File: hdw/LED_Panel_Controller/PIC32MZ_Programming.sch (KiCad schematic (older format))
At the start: 17 parts

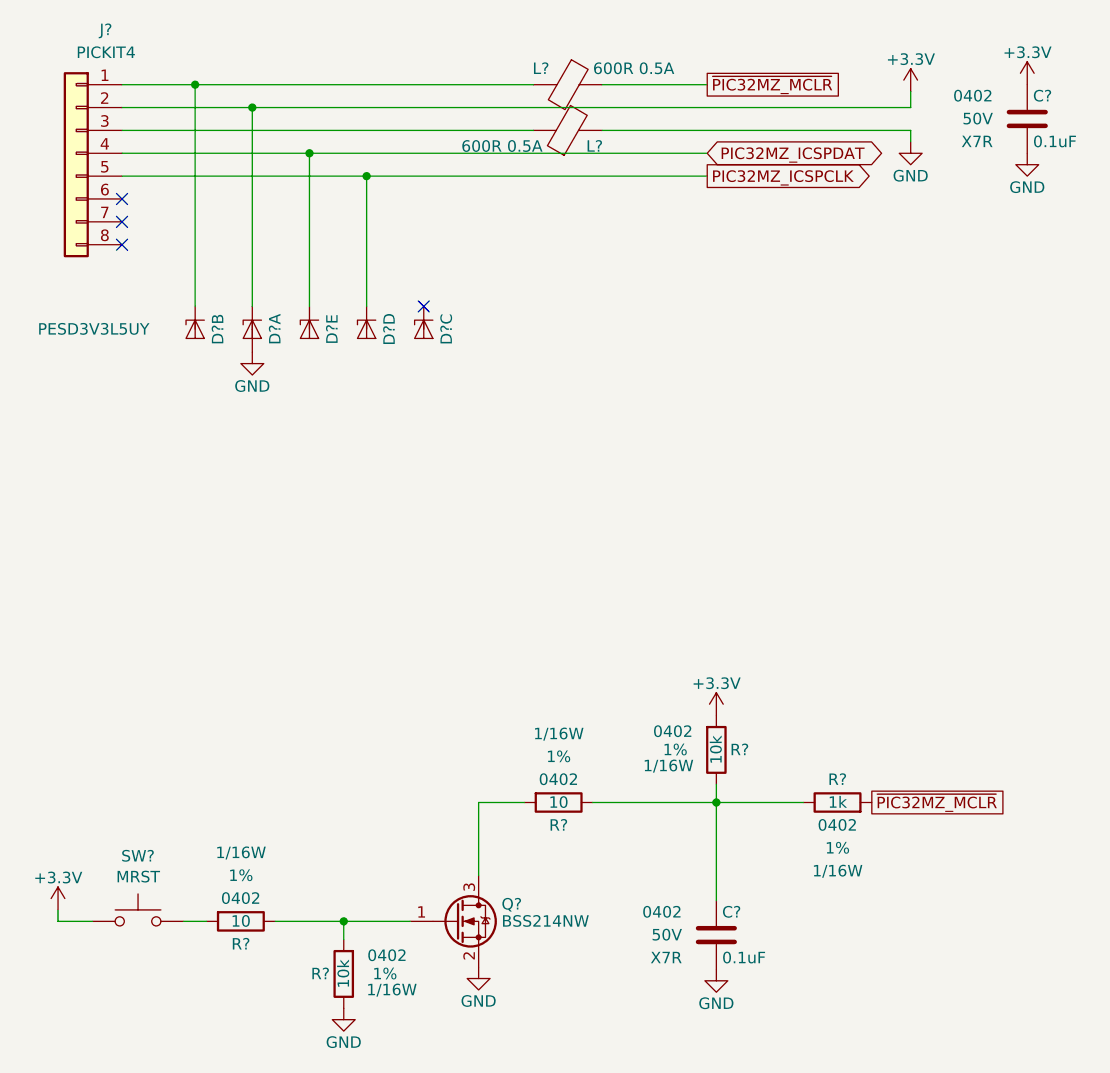
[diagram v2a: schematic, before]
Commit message: added digikey pns, footprints, bom scrubbed
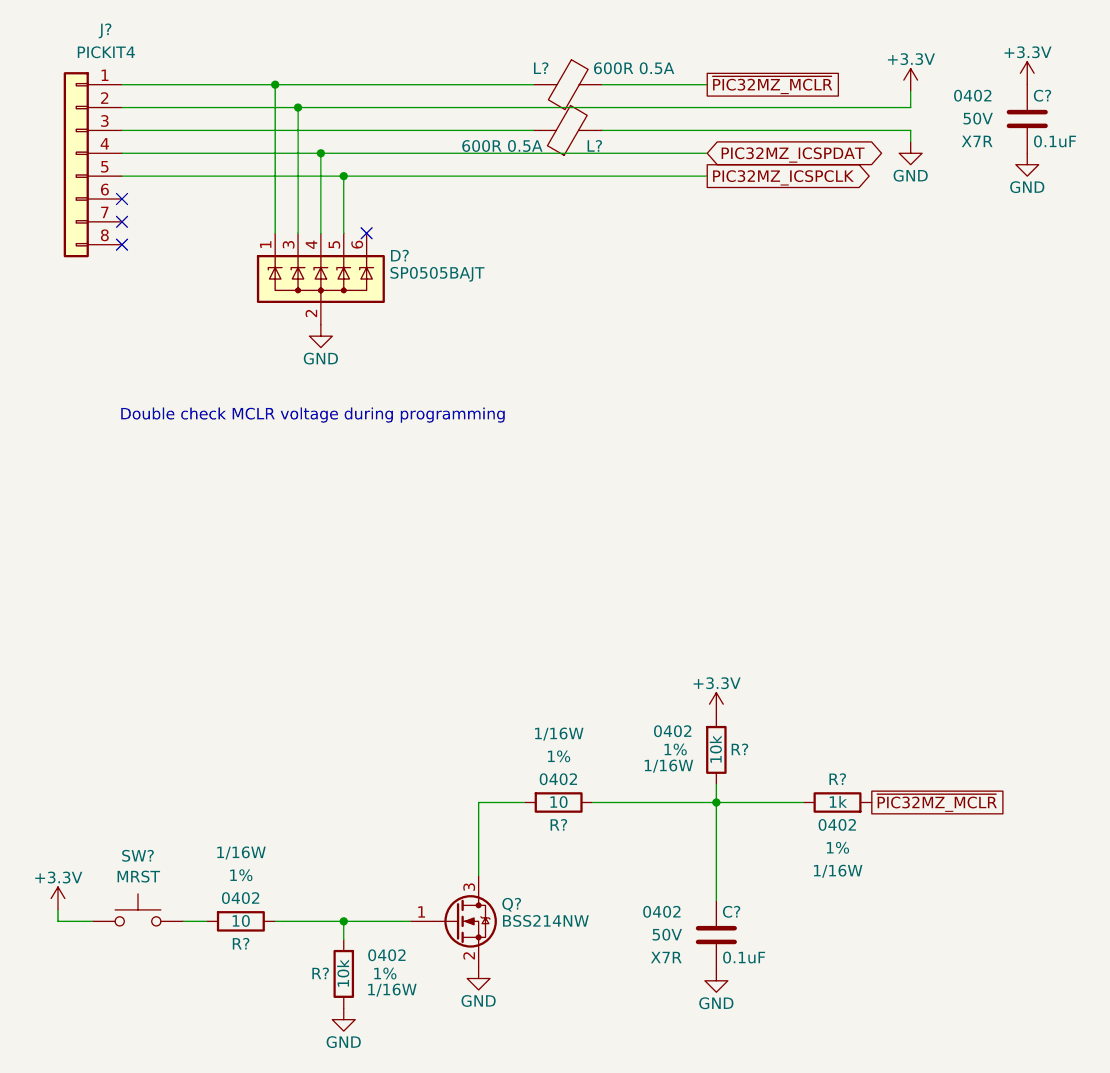
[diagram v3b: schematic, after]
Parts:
- removed D? (x5): PESD3V3L5UY, Package_TO_SOT_SMD:SOT-363_SC-70-6, symbol Power_Protection:PESD3V3L5UY
- added D?: SP0505BAJT, TO_SOT_Packages_SMD:SOT-363_SC-70-6, symbol Power_Protection:SP0505BAJT
- C? (x2): footprint (none) -> Capacitors_SMD:C_0402; Digi-Key PN (none) -> 490-10701-1-ND
- J?: Configuration (none) -> DEV
- R? (x2): Digi-Key PN (none) -> RMCF0402FT10K0CT-ND
- R?: Digi-Key PN (none) -> RMCF0402FT1K00CT-ND
- R? (x2): Digi-Key PN (none) -> RMCF0402FT10R0CT-ND
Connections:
- net +3V3: now also D?.3 (K)
- net GND: now also D?.2 (A)
- net PIC32MZ_ICSPCLK: now also D?.5 (K)
- net PIC32MZ_ICSPDAT: now also D?.4 (K)
- net at J?.1 (Pin_1), L?.2: now also D?.1 (K)
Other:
- note added: "Double check MCLR voltage during programming"
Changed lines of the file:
@@
 F 0 "C?" H 7155 2110 50  0000 L CNN
 F 1 "0.1uF" H 7155 1910 50  0000 L CNN
-F 2 "" H 7168 1860 50  0001 C CNN
+F 2 "Capacitors_SMD:C_0402" H 7168 1860 50  0001 C CNN
 F 3 "" H 7155 2110 50  0001 C CNN
 F 4 "0402" H 6980 2110 50  0000 R CNN "display_footprint"
 F 5 "50V" H 6980 2010 50  0000 R CNN "Voltage"
 F 6 "X7R" H 6980 1910 50  0000 R CNN "Dielectric"
-F 7 "" H 7555 2510 60  0001 C CNN "Digi-Key PN"
+F 7 "490-10701-1-ND" H 7555 2510 60  0001 C CNN "Digi-Key PN"
 	1    7130 2010
 	1    0    0    -1
@@
 F 5 "1%" H 5950 4770 50  0000 C CNN "Tolerance"
 F 6 "1/16W" H 5980 4700 50  0000 C CNN "Wattage"
-F 7 "" H 6070 5170 60  0001 C CNN "Digi-Key PN"
+F 7 "RMCF0402FT10K0CT-ND" H 6070 5170 60  0001 C CNN "Digi-Key PN"
 	1    5770 4770
 	-1   0    0    -1
@@
 F 0 "C?" H 5795 5680 50  0000 L CNN
 F 1 "0.1uF" H 5795 5480 50  0000 L CNN
-F 2 "" H 5808 5430 50  0001 C CNN
+F 2 "Capacitors_SMD:C_0402" H 5808 5430 50  0001 C CNN
 F 3 "" H 5795 5680 50  0001 C CNN
 F 4 "0402" H 5620 5680 50  0000 R CNN "display_footprint"
 F 5 "50V" H 5620 5580 50  0000 R CNN "Voltage"
 F 6 "X7R" H 5620 5480 50  0000 R CNN "Dielectric"
-F 7 "" H 6195 6080 60  0001 C CNN "Digi-Key PN"
+F 7 "490-10701-1-ND" H 6195 6080 60  0001 C CNN "Digi-Key PN"
 	1    5770 5580
 	1    0    0    -1
@@
 F 5 "1%" V 6500 5000 50  0000 C CNN "Tolerance"
 F 6 "1/16W" V 6600 5000 50  0000 C CNN "Wattage"
-F 7 "" H 6600 5400 60  0001 C CNN "Digi-Key PN"
+F 7 "RMCF0402FT1K00CT-ND" H 6600 5400 60  0001 C CNN "Digi-Key PN"
 	1    6300 5000
 	0    1    1    0
@@
 F 5 "1%" V 3890 5520 50  0000 C CNN "Tolerance"
 F 6 "1/16W" V 3990 5520 50  0000 C CNN "Wattage"
-F 7 "" H 3990 5920 60  0001 C CNN "Digi-Key PN"
+F 7 "RMCF0402FT10R0CT-ND" H 3990 5920 60  0001 C CNN "Digi-Key PN"
 	1    3690 5520
 	0    -1   -1   0
@@
 F 5 "1%" H 4320 5750 50  0000 C CNN "Tolerance"
 F 6 "1/16W" H 4350 5680 50  0000 C CNN "Wattage"
-F 7 "" H 4440 6150 60  0001 C CNN "Digi-Key PN"
+F 7 "RMCF0402FT10K0CT-ND" H 4440 6150 60  0001 C CNN "Digi-Key PN"
 	1    4140 5750
 	1    0    0    -1
@@
 F 2 "Custom Footprints Library:PICKIT4_Header" H 2970 2160 50  0001 C CNN
 F 3 "~" H 2970 2160 50  0001 C CNN
+F 4 "DEV" H 2970 2160 50  0001 C CNN "Configuration"
 	1    2970 2160
 	-1   0    0    -1
@@
 NoConn ~ 3170 2460
 NoConn ~ 3170 2560
-$Comp
-L Power_Protection:PESD3V3L5UY D?
-U 1 1 5F37FACB
-P 3740 2930
-F 0 "D?" H 3740 3030 50  0000 C CNN
-F 1 "PESD3V3L5UY" V 3740 2480 50  0000 R CNN
-F 2 "Package_TO_SOT_SMD:SOT-363_SC-70-6" H 3740 2930 50  0001 C CNN
-F 3 "https://assets.nexperia.com/documents/data-sheet/PESDXL5UF_V_Y.pdf" H 3740 2930 50  0001 C CNN
-F 4 "1727-3828-1-ND" H 3740 2930 50  0001 C CNN "Digi-Key PN"
-	1    3740 2930
-	0    1    1    0
-$EndComp
-$Comp
-L Power_Protection:PESD3V3L5UY D?
-U 3 1 5F380F72
-P 4490 2930
-F 0 "D?" H 4490 3030 50  0000 C CNN
-F 1 "PESD3V3L5UY" H 4490 2830 50  0001 C CNN
-F 2 "Package_TO_SOT_SMD:SOT-363_SC-70-6" H 4490 2930 50  0001 C CNN
-F 3 "https://assets.nexperia.com/documents/data-sheet/PESDXL5UF_V_Y.pdf" H 4490 2930 50  0001 C CNN
-F 4 "1727-3828-1-ND" H 4490 2930 50  0001 C CNN "Digi-Key PN"
-	3    4490 2930
-	0    1    1    0
-$EndComp
-$Comp
-L Power_Protection:PESD3V3L5UY D?
-U 4 1 5F381590
-P 4240 2930
-F 0 "D?" H 4240 3030 50  0000 C CNN
-F 1 "PESD3V3L5UY" H 4240 2830 50  0001 C CNN
-F 2 "Package_TO_SOT_SMD:SOT-363_SC-70-6" H 4240 2930 50  0001 C CNN
-F 3 "https://assets.nexperia.com/documents/data-sheet/PESDXL5UF_V_Y.pdf" H 4240 2930 50  0001 C CNN
-F 4 "1727-3828-1-ND" H 4240 2930 50  0001 C CNN "Digi-Key PN"
-	4    4240 2930
-	0    1    1    0
-$EndComp
-$Comp
-L power:GND #PWR?
-U 1 1 5F3831ED
-P 3740 3030
-F 0 "#PWR?" H 3740 2780 50  0001 C CNN
-F 1 "GND" H 3740 2880 50  0000 C CNN
-F 2 "" H 3740 3030 50  0001 C CNN
-F 3 "" H 3740 3030 50  0001 C CNN
-	1    3740 3030
-	-1   0    0    -1
-$EndComp
 $Comp
 L Device:Ferrite_Bead L?
@@
 	5270 2060 6620 2060
 Wire Wire Line
-	3170 1960 3740 1960
-Wire Wire Line
-	3170 1860 3490 1860
-Wire Wire Line
-	3170 2160 3990 2160
-Wire Wire Line
-	3490 2830 3490 1860
-Wire Wire Line
-	3740 2830 3740 1960
-Wire Wire Line
-	3990 2830 3990 2160
-Wire Wire Line
-	4240 2830 4240 2260
-Wire Wire Line
-	4240 2260 3170 2260
-NoConn ~ 4490 2830
-Wire Wire Line
-	3490 1860 4970 1860
-Connection ~ 3490 1860
-Wire Wire Line
-	3740 1960 6620 1960
-Connection ~ 3740 1960
-Wire Wire Line
 	4970 2060 3170 2060
-Wire Wire Line
-	3990 2160 5730 2160
-Connection ~ 3990 2160
-Wire Wire Line
-	5730 2260 4240 2260
-Connection ~ 4240 2260
 Wire Wire Line
 	4730 5000 4930 5000
@@
 F 5 "1%" V 5280 5000 50  0000 C CNN "Tolerance"
 F 6 "1/16W" V 5380 5000 50  0000 C CNN "Wattage"
-F 7 "" H 5380 5400 60  0001 C CNN "Digi-Key PN"
+F 7 "RMCF0402FT10R0CT-ND" H 5380 5400 60  0001 C CNN "Digi-Key PN"
 	1    5080 5000
 	0    -1   -1   0
 $EndComp
-$Comp
-L Power_Protection:PESD3V3L5UY D?
-U 5 1 5F39050C
-P 3990 2930
-F 0 "D?" H 3990 3030 50  0000 C CNN
-F 1 "PESD3V3L5UY" H 3990 2830 50  0001 C CNN
-F 2 "Package_TO_SOT_SMD:SOT-363_SC-70-6" H 3990 2930 50  0001 C CNN
-F 3 "https://assets.nexperia.com/documents/data-sheet/PESDXL5UF_V_Y.pdf" H 3990 2930 50  0001 C CNN
-F 4 "1727-3828-1-ND" H 3990 2930 50  0001 C CNN "Digi-Key PN"
-	5    3990 2930
-	0    1    1    0
-$EndComp
-$Comp
-L Power_Protection:PESD3V3L5UY D?
-U 2 1 5F38087E
-P 3490 2930
-F 0 "D?" H 3490 3030 50  0000 C CNN
-F 1 "PESD3V3L5UY" H 3490 2830 50  0001 C CNN
-F 2 "Package_TO_SOT_SMD:SOT-363_SC-70-6" H 3490 2930 50  0001 C CNN
-F 3 "https://assets.nexperia.com/documents/data-sheet/PESDXL5UF_V_Y.pdf" H 3490 2930 50  0001 C CNN
-F 4 "1727-3828-1-ND" H 3490 2930 50  0001 C CNN "Digi-Key PN"
-	2    3490 2930
-	0    1    1    0
-$EndComp
+Wire Wire Line
+	3170 2160 4040 2160
+Wire Wire Line
+	3170 2260 4140 2260
+$Comp
+L Power_Protection:SP0505BAJT D?
+U 1 1 6067D672
+P 4040 2710
+AR Path="/5F583BFC/6067D672" Ref="D?"  Part="1"
+AR Path="/5F5829A6/6067D672" Ref="D?"  Part="1"
+F 0 "D?" H 4340 2810 50  0000 L CNN
+F 1 "SP0505BAJT" H 4340 2735 50  0000 L CNN
+F 2 "TO_SOT_Packages_SMD:SOT-363_SC-70-6" H 4340 2660 50  0001 L CNN
+F 3 "http://www.littelfuse.com/~/media/files/littelfuse/technical%20resources/documents/data%20sheets/sp05xxba.pdf" H 4165 2835 50  0001 C CNN
+F 4 "F3160CT-ND" H 4040 2710 50  0001 C CNN "Digi-Key PN"
+	1    4040 2710
+	1    0    0    -1
+$EndComp
+$Comp
+L power:GND #PWR?
+U 1 1 6067E0F5
+P 4040 2910
+F 0 "#PWR?" H 4040 2660 50  0001 C CNN
+F 1 "GND" H 4040 2760 50  0000 C CNN
+F 2 "" H 4040 2910 50  0001 C CNN
+F 3 "" H 4040 2910 50  0001 C CNN
+	1    4040 2910
+	1    0    0    -1
+$EndComp
+Wire Wire Line
+	3170 1860 3840 1860
+Wire Wire Line
+	3170 1960 3940 1960
+Wire Wire Line
+	3940 2510 3940 1960
+Connection ~ 3940 1960
+Wire Wire Line
+	3940 1960 6620 1960
+Wire Wire Line
+	4040 2510 4040 2160
+Connection ~ 4040 2160
+Wire Wire Line
+	4040 2160 5730 2160
+Wire Wire Line
+	4140 2510 4140 2260
+Connection ~ 4140 2260
+Wire Wire Line
+	4140 2260 5730 2260
+Wire Wire Line
+	3840 2510 3840 1860
+Connection ~ 3840 1860
+Wire Wire Line
+	3840 1860 4970 1860
+NoConn ~ 4240 2510
+Text Notes 3160 3340 0    50   ~ 0
+Double check MCLR voltage during programming
 $EndSCHEMATC

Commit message: assigned I2C addresses
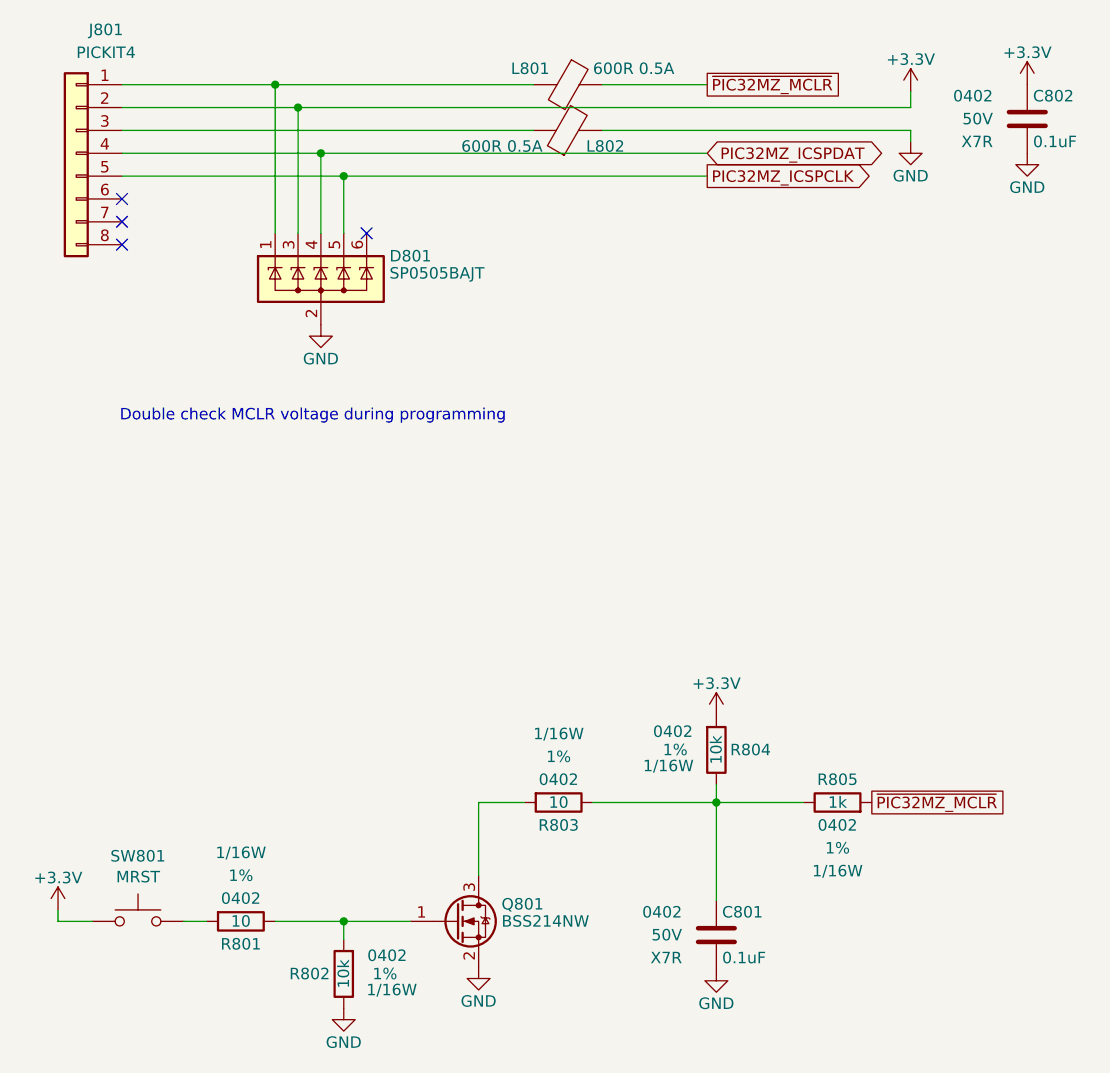
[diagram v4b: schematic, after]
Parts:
- gave numbers to parts that had none: 13
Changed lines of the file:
@@
 PIC32MZ_ICSPCLK
 $Comp
-L power:GND #PWR?
+L power:GND #PWR0808
 U 1 1 5BB4A7C4
 P 6620 2110
-F 0 "#PWR?" H 6620 1860 50  0001 C CNN
+F 0 "#PWR0808" H 6620 1860 50  0001 C CNN
 F 1 "GND" H 6620 1960 50  0000 C CNN
 F 2 "" H 6620 2110 50  0001 C CNN
@@
 NoConn ~ 3170 2360
 $Comp
-L Custom_Library:C_Custom C?
+L Custom_Library:C_Custom C802
 U 1 1 5BC13497
 P 7130 2010
-F 0 "C?" H 7155 2110 50  0000 L CNN
+F 0 "C802" H 7155 2110 50  0000 L CNN
 F 1 "0.1uF" H 7155 1910 50  0000 L CNN
 F 2 "Capacitors_SMD:C_0402" H 7168 1860 50  0001 C CNN
@@
 $EndComp
 $Comp
-L power:GND #PWR?
+L power:GND #PWR0810
 U 1 1 5BC1349E
 P 7130 2160
-F 0 "#PWR?" H 7130 1910 50  0001 C CNN
+F 0 "#PWR0810" H 7130 1910 50  0001 C CNN
 F 1 "GND" H 7130 2010 50  0000 C CNN
 F 2 "" H 7130 2160 50  0001 C CNN
@@
 AR Path="/5EAE2EF2/5BC152E5" Ref="R?"  Part="1"
 AR Path="/5E939EAF/5BC152E5" Ref="R?"  Part="1"
-AR Path="/5F5829A6/5BC152E5" Ref="R?"  Part="1"
-F 0 "R?" H 5710 4770 50  0000 R CNN
+AR Path="/5F5829A6/5BC152E5" Ref="R804"  Part="1"
+F 0 "R804" H 5710 4770 50  0000 R CNN
 F 1 "10k" V 5770 4770 50  0000 C CNN
 F 2 "Resistors_SMD:R_0402" H 5770 4770 50  0001 C CNN
@@
 $EndComp
 $Comp
-L Custom_Library:C_Custom C?
+L Custom_Library:C_Custom C801
 U 1 1 5BC1574E
 P 5770 5580
-F 0 "C?" H 5795 5680 50  0000 L CNN
+F 0 "C801" H 5795 5680 50  0000 L CNN
 F 1 "0.1uF" H 5795 5480 50  0000 L CNN
 F 2 "Capacitors_SMD:C_0402" H 5808 5430 50  0001 C CNN
@@
 $EndComp
 $Comp
-L power:GND #PWR?
+L power:GND #PWR0806
 U 1 1 5BC15E18
 P 5770 5730
-F 0 "#PWR?" H 5770 5480 50  0001 C CNN
+F 0 "#PWR0806" H 5770 5480 50  0001 C CNN
 F 1 "GND" H 5770 5580 50  0000 C CNN
 F 2 "" H 5770 5730 50  0001 C CNN
@@
 $EndComp
 $Comp
-L Custom_Library:R_Custom R?
+L Custom_Library:R_Custom R805
 U 1 1 5BC16316
 P 6300 5000
-F 0 "R?" V 6200 5000 50  0000 C CNN
+F 0 "R805" V 6200 5000 50  0000 C CNN
 F 1 "1k" V 6300 5000 50  0000 C CNN
 F 2 "Resistors_SMD:R_0402" H 6300 5000 50  0001 C CNN
@@
 ~PIC32MZ_MCLR
 $Comp
-L Switch:SW_Push SW?
+L Switch:SW_Push SW801
 U 1 1 5BC17B44
 P 3240 5520
-F 0 "SW?" H 3240 5805 50  0000 C CNN
+F 0 "SW801" H 3240 5805 50  0000 C CNN
 F 1 "MRST" H 3240 5714 50  0000 C CNN
 F 2 "Buttons_Switches_THT:SW_PUSH_6mm" H 3240 5720 50  0001 C CNN
@@
 $EndComp
 $Comp
-L power:GND #PWR?
+L power:GND #PWR0804
 U 1 1 5BE087C1
 P 4730 5720
-F 0 "#PWR?" H 4730 5470 50  0001 C CNN
+F 0 "#PWR0804" H 4730 5470 50  0001 C CNN
 F 1 "GND" H 4730 5570 50  0000 C CNN
 F 2 "" H 4730 5720 50  0001 C CNN
@@
 $EndComp
 $Comp
-L Custom_Library:R_Custom R?
+L Custom_Library:R_Custom R801
 U 1 1 5BE087CB
 P 3690 5520
-F 0 "R?" V 3590 5520 50  0000 C CNN
+F 0 "R801" V 3590 5520 50  0000 C CNN
 F 1 "10" V 3690 5520 50  0000 C CNN
 F 2 "Resistors_SMD:R_0402" H 3690 5520 50  0001 C CNN
@@
 AR Path="/5EAE2EF2/5BE087D6" Ref="R?"  Part="1"
 AR Path="/5E939EAF/5BE087D6" Ref="R?"  Part="1"
-AR Path="/5F5829A6/5BE087D6" Ref="R?"  Part="1"
-F 0 "R?" H 4080 5750 50  0000 R CNN
+AR Path="/5F5829A6/5BE087D6" Ref="R802"  Part="1"
+F 0 "R802" H 4080 5750 50  0000 R CNN
 F 1 "10k" V 4140 5750 50  0000 C CNN
 F 2 "Resistors_SMD:R_0402" H 4140 5750 50  0001 C CNN
@@
 $EndComp
 $Comp
-L power:GND #PWR?
+L power:GND #PWR0803
 U 1 1 5BE087DD
 P 4140 5900
-F 0 "#PWR?" H 4140 5650 50  0001 C CNN
+F 0 "#PWR0803" H 4140 5650 50  0001 C CNN
 F 1 "GND" H 4140 5750 50  0000 C CNN
 F 2 "" H 4140 5900 50  0001 C CNN
@@
 	5770 5430 5770 5000
 $Comp
-L power:+3.3V #PWR?
+L power:+3.3V #PWR0801
 U 1 1 5E6EB62A
 P 2890 5470
-F 0 "#PWR?" H 2890 5320 50  0001 C CNN
+F 0 "#PWR0801" H 2890 5320 50  0001 C CNN
 F 1 "+3.3V" H 2890 5610 50  0000 C CNN
 F 2 "" H 2890 5470 50  0001 C CNN
@@
 $EndComp
 $Comp
-L power:+3.3V #PWR?
+L power:+3.3V #PWR0805
 U 1 1 5E6EBFA5
 P 5770 4620
-F 0 "#PWR?" H 5770 4470 50  0001 C CNN
+F 0 "#PWR0805" H 5770 4470 50  0001 C CNN
 F 1 "+3.3V" H 5770 4760 50  0000 C CNN
 F 2 "" H 5770 4620 50  0001 C CNN
@@
 $EndComp
 $Comp
-L power:+3.3V #PWR?
+L power:+3.3V #PWR0809
 U 1 1 5E6EC62F
 P 7130 1860
-F 0 "#PWR?" H 7130 1710 50  0001 C CNN
+F 0 "#PWR0809" H 7130 1710 50  0001 C CNN
 F 1 "+3.3V" H 7130 2000 50  0000 C CNN
 F 2 "" H 7130 1860 50  0001 C CNN
@@
 $EndComp
 $Comp
-L power:+3.3V #PWR?
+L power:+3.3V #PWR0807
 U 1 1 5E6ECA36
 P 6620 1890
-F 0 "#PWR?" H 6620 1740 50  0001 C CNN
+F 0 "#PWR0807" H 6620 1740 50  0001 C CNN
 F 1 "+3.3V" H 6620 2030 50  0000 C CNN
 F 2 "" H 6620 1890 50  0001 C CNN
@@
 $EndComp
 $Comp
-L Transistor_FET:BSS214NW Q?
+L Transistor_FET:BSS214NW Q801
 U 1 1 5E765004
 P 4630 5520
-F 0 "Q?" H 4830 5595 50  0000 L CNN
+F 0 "Q801" H 4830 5595 50  0000 L CNN
 F 1 "BSS214NW" H 4830 5520 50  0000 L CNN
 F 2 "Package_TO_SOT_SMD:SOT-323_SC-70" H 4830 5445 50  0001 L CIN
@@
 $EndComp
 $Comp
-L Connector_Generic:Conn_01x08 J?
+L Connector_Generic:Conn_01x08 J801
 U 1 1 5F36CE98
 P 2970 2160
-F 0 "J?" H 2840 2700 50  0000 C CNN
+F 0 "J801" H 2840 2700 50  0000 C CNN
 F 1 "PICKIT4" H 2840 2600 50  0000 C CNN
 F 2 "Custom Footprints Library:PICKIT4_Header" H 2970 2160 50  0001 C CNN
@@
 AR Path="/5E939EC2/5F386594" Ref="L?"  Part="1"
 AR Path="/5E939EAF/5F386594" Ref="L?"  Part="1"
-AR Path="/5F5829A6/5F386594" Ref="L?"  Part="1"
-F 0 "L?" V 5050 1780 50  0000 R CNN
+AR Path="/5F5829A6/5F386594" Ref="L801"  Part="1"
+F 0 "L801" V 5050 1780 50  0000 R CNN
 F 1 "600R 0.5A" V 5050 1970 50  0000 L CNN
 F 2 "Inductors_SMD:L_0402" V 5050 1860 50  0001 C CNN
@@
 AR Path="/5E939EC2/5F387C18" Ref="L?"  Part="1"
 AR Path="/5E939EAF/5F387C18" Ref="L?"  Part="1"
-AR Path="/5F5829A6/5F387C18" Ref="L?"  Part="1"
-F 0 "L?" V 5050 1980 50  0000 R CNN
+AR Path="/5F5829A6/5F387C18" Ref="L802"  Part="1"
+F 0 "L802" V 5050 1980 50  0000 R CNN
 F 1 "600R 0.5A" V 5050 2170 50  0000 L CNN
 F 2 "Inductors_SMD:L_0402" V 5050 2060 50  0001 C CNN
@@
 	5230 5000 5770 5000
 $Comp
-L Custom_Library:R_Custom R?
+L Custom_Library:R_Custom R803
 U 1 1 5EB9A4D9
 P 5080 5000
-F 0 "R?" V 4980 5000 50  0000 C CNN
+F 0 "R803" V 4980 5000 50  0000 C CNN
 F 1 "10" V 5080 5000 50  0000 C CNN
 F 2 "Resistors_SMD:R_0402" H 5080 5000 50  0001 C CNN
@@
 P 4040 2710
 AR Path="/5F583BFC/6067D672" Ref="D?"  Part="1"
-AR Path="/5F5829A6/6067D672" Ref="D?"  Part="1"
-F 0 "D?" H 4340 2810 50  0000 L CNN
+AR Path="/5F5829A6/6067D672" Ref="D801"  Part="1"
+F 0 "D801" H 4340 2810 50  0000 L CNN
 F 1 "SP0505BAJT" H 4340 2735 50  0000 L CNN
 F 2 "TO_SOT_Packages_SMD:SOT-363_SC-70-6" H 4340 2660 50  0001 L CNN
@@
 $EndComp
 $Comp
-L power:GND #PWR?
+L power:GND #PWR0802
 U 1 1 6067E0F5
 P 4040 2910
-F 0 "#PWR?" H 4040 2660 50  0001 C CNN
+F 0 "#PWR0802" H 4040 2660 50  0001 C CNN
 F 1 "GND" H 4040 2760 50  0000 C CNN
 F 2 "" H 4040 2910 50  0001 C CNN
